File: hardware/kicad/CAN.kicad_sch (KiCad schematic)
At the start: 0 parts

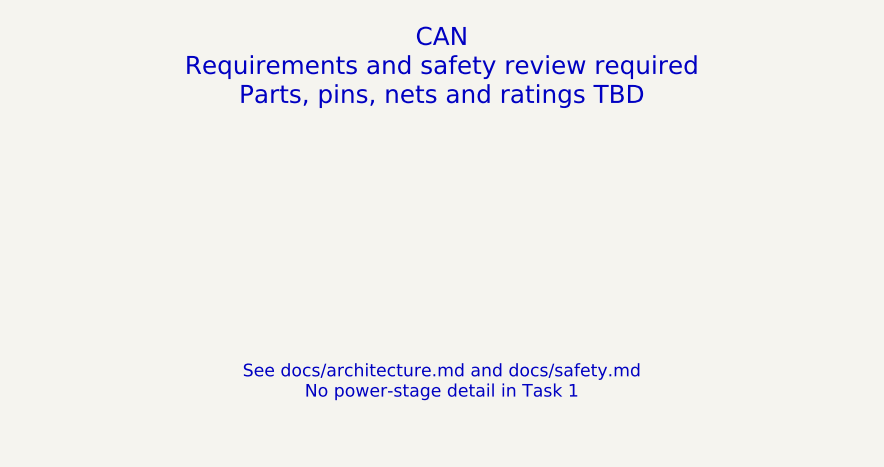
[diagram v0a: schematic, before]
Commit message: hardware: update existing KiCad architecture and add precharge sheet
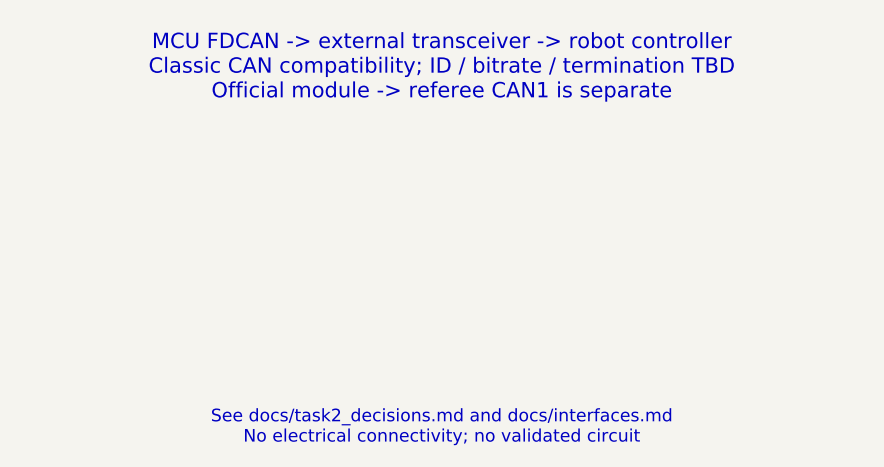
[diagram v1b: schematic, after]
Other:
- note added: "MCU FDCAN -> external transceiver -> robot controller Classic CAN compatibility; ID / bitrate / termination TBD Official module -> referee CAN1 is separate"
- note added: "See docs/task2_decisions.md and docs/interfaces.md No electrical connectivity; no validated circuit"
- note removed: "CAN Requirements and safety review required Parts, pins, nets and ratings TBD"
- note removed: "See docs/architecture.md and docs/safety.md No power-stage detail in Task 1"
- title: CAN - Placeholder -> CAN - Task 2 Proposal

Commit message: hardware: implement prototype Rev A electrical schematic
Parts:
- added C81: 100nF / 16V X7R, Capacitor_SMD:C_0805_2012Metric, symbol RevA:C
- added J19: robot telemetry CAN / official module CAN separate, symbol RevA:J3
- added J20: selectable termination shunt, fit only at bus end, Connector_PinHeader_2.54mm:PinHeader_1x02_P2.54mm_Vertical, symbol RevA:J2
- added R161, R162: 10k, Resistor_SMD:R_0805_2012Metric, symbol RevA:R
- added R163: 120R /1%, Resistor_SMD:R_0805_2012Metric, symbol RevA:R
- added U27: SN65HVD230DR, Package_SO:SOIC-8_3.9x4.9mm_P1.27mm, symbol RevA:SN65HVD230DR
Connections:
- new net CAN_H: J19.1 (P1), R163.1 (A), U27.7 (CANH)
- new net CAN_L: J19.2 (P2), J20.2 (P2), U27.6 (CANL)
- new net CAN_RX: U27.4 (R)
- new net CAN_STANDBY: R162.1 (A), U27.8 (RS)
- new net CAN_TERM: J20.1 (P1), R163.2 (B)
- new net CAN_TX: R161.1 (A), U27.1 (D)
- new net GND: C81.2 (B), J19.3 (P3), U27.2 (GND)
- new net V3V3: C81.1 (A), R161.2 (B), R162.2 (B), U27.3 (VCC)
- no-connect marks 0 -> 1
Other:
- note added: "CAN powered-off impedance/common-mode protection and external power through UART/SWD/taps require validation."
- note added: "Classic CAN initial protocol, bitrate/ID/timeouts TBD. CAN comm must not bypass official cutoff."
- note removed: "MCU FDCAN -> external transceiver -> robot controller Classic CAN compatibility; ID / bitrate / termination TBD Official module -> referee CAN1 is separate"
- note removed: "See docs/task2_decisions.md and docs/interfaces.md No electrical connectivity; no validated circuit"
- title: CAN - Task 2 Proposal -> CAN / Prototype Rev A draft

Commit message: hardware: refine Rev A protection and passive selections
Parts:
- removed C81: 100nF / 16V X7R, Capacitor_SMD:C_0805_2012Metric, symbol RevA:C
- removed J19: robot telemetry CAN / official module CAN separate, symbol RevA:J3
- removed J20: selectable termination shunt, fit only at bus end, Connector_PinHeader_2.54mm:PinHeader_1x02_P2.54mm_Vertical, symbol RevA:J2
- removed R161, R162: 10k, Resistor_SMD:R_0805_2012Metric, symbol RevA:R
- removed R163: 120R /1%, Resistor_SMD:R_0805_2012Metric, symbol RevA:R
- removed U27: SN65HVD230DR, Package_SO:SOIC-8_3.9x4.9mm_P1.27mm, symbol RevA:SN65HVD230DR
- added C99: 100nF / 16V X7R, Capacitor_SMD:C_0805_2012Metric, symbol RevA:C
- added J16: robot telemetry CAN / official module CAN separate, symbol RevA:J3
- added J17: selectable termination shunt, fit only at bus end, Connector_PinHeader_2.54mm:PinHeader_1x02_P2.54mm_Vertical, symbol RevA:J2
- added R167, R168: 10k, Resistor_SMD:R_0805_2012Metric, symbol RevA:R
- added R169: 120R /1%, Resistor_SMD:R_0805_2012Metric, symbol RevA:R
- added U33: SN65HVD230DR, Package_SO:SOIC-8_3.9x4.9mm_P1.27mm, symbol RevA:SN65HVD230DR
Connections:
- net CAN_H: now also J16.1 (P1), R169.1 (A), U33.7 (CANH)
- net CAN_L: now also J16.2 (P2), J17.2 (P2), U33.6 (CANL)
- net CAN_RX: now also U33.4 (R)
- net CAN_STANDBY: now also R168.1 (A), U33.8 (RS)
- net CAN_TERM: now also J17.1 (P1), R169.2 (B)
- net CAN_TX: now also R167.1 (A), U33.1 (D)
- net GND: now also C99.2 (B), J16.3 (P3), U33.2 (GND)
- net V3V3: now also C99.1 (A), R167.2 (B), R168.2 (B), U33.3 (VCC)
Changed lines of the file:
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@@
     (on_board yes)
     (dnp no)
-    (property "Reference" "U27" (at 88.9 102.95 0) (effects (font (size 1 1))))
+    (property "Reference" "U33" (at 88.9 102.95 0) (effects (font (size 1 1))))
     (property "Value" "SN65HVD230DR" (at 88.9 124.64999999999999 0) (effects (font (size 1 1))))
     (property "Footprint" "Package_SO:SOIC-8_3.9x4.9mm_P1.27mm" (at 88.9 114.3 0) (effects (font (size 1 1))) (hide yes))
     (property "Datasheet" "https://www.ti.com/lit/ds/symlink/sn65hvd230.pdf" (at 88.9 114.3 0) (effects (font (size 1 1))) (hide yes))
+    (property "MPN" "SN65HVD230DR" (at 88.9 114.3 0) (effects (font (size 1 1))) (hide yes))
     (pin "1")
     (pin "2")
@@
     (pin "7")
     (pin "8")
-    (instances (project "robomaster_supercap" (path "/fe0d835f-f536-483b-a54a-4b6f1f4699ec/f2d4b9a7-1a6d-5805-a86e-ee030607ac49" (reference "U27") (unit 1))))
+    (instances (project "robomaster_supercap" (path "/fe0d835f-f536-483b-a54a-4b6f1f4699ec/f2d4b9a7-1a6d-5805-a86e-ee030607ac49" (reference "U33") (unit 1))))
   )
   (wire (pts (xy 73.66 110.49) (xy 68.58 110.49)) (stroke (width 0) (type default)))
@@
     (on_board yes)
     (dnp no)
-    (property "Reference" "C81" (at 241.3 104.3 0) (effects (font (size 1 1))))
+    (property "Reference" "C99" (at 241.3 104.3 0) (effects (font (size 1 1))))
     (property "Value" "100nF / 16V X7R" (at 241.3 123.3 0) (effects (font (size 1 1))))
     (property "Footprint" "Capacitor_SMD:C_0805_2012Metric" (at 241.3 114.3 0) (effects (font (size 1 1))) (hide yes))
     (property "Datasheet" "" (at 241.3 114.3 0) (effects (font (size 1 1))) (hide yes))
+    (property "MPN" "C0805C104K5RACTU" (at 241.3 114.3 0) (effects (font (size 1 1))) (hide yes))
     (pin "1")
     (pin "2")
-    (instances (project "robomaster_supercap" (path "/fe0d835f-f536-483b-a54a-4b6f1f4699ec/f2d4b9a7-1a6d-5805-a86e-ee030607ac49" (reference "C81") (unit 1))))
+    (instances (project "robomaster_supercap" (path "/fe0d835f-f536-483b-a54a-4b6f1f4699ec/f2d4b9a7-1a6d-5805-a86e-ee030607ac49" (reference "C99") (unit 1))))
   )
   (wire (pts (xy 226.06 114.3) (xy 220.98 114.3)) (stroke (width 0) (type default)))
@@
     (on_board yes)
     (dnp no)
-    (property "Reference" "R161" (at 393.70000000000005 104.3 0) (effects (font (size 1 1))))
+    (property "Reference" "R167" (at 393.70000000000005 104.3 0) (effects (font (size 1 1))))
     (property "Value" "10k" (at 393.70000000000005 123.3 0) (effects (font (size 1 1))))
     (property "Footprint" "Resistor_SMD:R_0805_2012Metric" (at 393.70000000000005 114.3 0) (effects (font (size 1 1))) (hide yes))
     (property "Datasheet" "" (at 393.70000000000005 114.3 0) (effects (font (size 1 1))) (hide yes))
+    (property "MPN" "CRCW080510K0FKEA" (at 393.70000000000005 114.3 0) (effects (font (size 1 1))) (hide yes))
     (pin "1")
     (pin "2")
-    (instances (project "robomaster_supercap" (path "/fe0d835f-f536-483b-a54a-4b6f1f4699ec/f2d4b9a7-1a6d-5805-a86e-ee030607ac49" (reference "R161") (unit 1))))
+    (instances (project "robomaster_supercap" (path "/fe0d835f-f536-483b-a54a-4b6f1f4699ec/f2d4b9a7-1a6d-5805-a86e-ee030607ac49" (reference "R167") (unit 1))))
   )
   (wire (pts (xy 378.46 114.3) (xy 373.38 114.3)) (stroke (width 0) (type default)))
@@
     (on_board yes)
     (dnp no)
-    (property "Reference" "R162" (at 546.1 104.3 0) (effects (font (size 1 1))))
+    (property "Reference" "R168" (at 546.1 104.3 0) (effects (font (size 1 1))))
     (property "Value" "10k" (at 546.1 123.3 0) (effects (font (size 1 1))))
     (property "Footprint" "Resistor_SMD:R_0805_2012Metric" (at 546.1 114.3 0) (effects (font (size 1 1))) (hide yes))
     (property "Datasheet" "" (at 546.1 114.3 0) (effects (font (size 1 1))) (hide yes))
+    (property "MPN" "CRCW080510K0FKEA" (at 546.1 114.3 0) (effects (font (size 1 1))) (hide yes))
     (pin "1")
     (pin "2")
-    (instances (project "robomaster_supercap" (path "/fe0d835f-f536-483b-a54a-4b6f1f4699ec/f2d4b9a7-1a6d-5805-a86e-ee030607ac49" (reference "R162") (unit 1))))
+    (instances (project "robomaster_supercap" (path "/fe0d835f-f536-483b-a54a-4b6f1f4699ec/f2d4b9a7-1a6d-5805-a86e-ee030607ac49" (reference "R168") (unit 1))))
   )
   (wire (pts (xy 530.86 114.3) (xy 525.78 114.3)) (stroke (width 0) (type default)))
@@
     (on_board yes)
     (dnp no)
-    (property "Reference" "J19" (at 698.5 104.3 0) (effects (font (size 1 1))))
+    (property "Reference" "J16" (at 698.5 104.3 0) (effects (font (size 1 1))))
     (property "Value" "robot telemetry CAN / official module CAN separate" (at 698.5 123.3 0) (effects (font (size 1 1))))
     (property "Footprint" "" (at 698.5 114.3 0) (effects (font (size 1 1))) (hide yes))
     (property "Datasheet" "" (at 698.5 114.3 0) (effects (font (size 1 1))) (hide yes))
+    (property "MPN" "" (at 698.5 114.3 0) (effects (font (size 1 1))) (hide yes))
     (pin "1")
     (pin "2")
     (pin "3")
-    (instances (project "robomaster_supercap" (path "/fe0d835f-f536-483b-a54a-4b6f1f4699ec/f2d4b9a7-1a6d-5805-a86e-ee030607ac49" (reference "J19") (unit 1))))
+    (instances (project "robomaster_supercap" (path "/fe0d835f-f536-483b-a54a-4b6f1f4699ec/f2d4b9a7-1a6d-5805-a86e-ee030607ac49" (reference "J16") (unit 1))))
   )
   (wire (pts (xy 683.26 113.03) (xy 678.18 113.03)) (stroke (width 0) (type default)))
@@
     (on_board yes)
     (dnp no)
-    (property "Reference" "R163" (at 850.9 104.3 0) (effects (font (size 1 1))))
+    (property "Reference" "R169" (at 850.9 104.3 0) (effects (font (size 1 1))))
     (property "Value" "120R /1%" (at 850.9 123.3 0) (effects (font (size 1 1))))
     (property "Footprint" "Resistor_SMD:R_0805_2012Metric" (at 850.9 114.3 0) (effects (font (size 1 1))) (hide yes))
     (property "Datasheet" "" (at 850.9 114.3 0) (effects (font (size 1 1))) (hide yes))
+    (property "MPN" "CRCW0805120RFKEA" (at 850.9 114.3 0) (effects (font (size 1 1))) (hide yes))
     (pin "1")
     (pin "2")
-    (instances (project "robomaster_supercap" (path "/fe0d835f-f536-483b-a54a-4b6f1f4699ec/f2d4b9a7-1a6d-5805-a86e-ee030607ac49" (reference "R163") (unit 1))))
+    (instances (project "robomaster_supercap" (path "/fe0d835f-f536-483b-a54a-4b6f1f4699ec/f2d4b9a7-1a6d-5805-a86e-ee030607ac49" (reference "R169") (unit 1))))
   )
   (wire (pts (xy 835.66 114.3) (xy 830.58 114.3)) (stroke (width 0) (type default)))
@@
     (on_board yes)
     (dnp no)
-    (property "Reference" "J20" (at 1003.3000000000001 104.3 0) (effects (font (size 1 1))))
+    (property "Reference" "J17" (at 1003.3000000000001 104.3 0) (effects (font (size 1 1))))
     (property "Value" "selectable termination shunt, fit only at bus end" (at 1003.3000000000001 123.3 0) (effects (font (size 1 1))))
     (property "Footprint" "Connector_PinHeader_2.54mm:PinHeader_1x02_P2.54mm_Vertical" (at 1003.3000000000001 114.3 0) (effects (font (size 1 1))) (hide yes))
     (property "Datasheet" "" (at 1003.3000000000001 114.3 0) (effects (font (size 1 1))) (hide yes))
+    (property "MPN" "" (at 1003.3000000000001 114.3 0) (effects (font (size 1 1))) (hide yes))
     (pin "1")
     (pin "2")
-    (instances (project "robomaster_supercap" (path "/fe0d835f-f536-483b-a54a-4b6f1f4699ec/f2d4b9a7-1a6d-5805-a86e-ee030607ac49" (reference "J20") (unit 1))))
+    (instances (project "robomaster_supercap" (path "/fe0d835f-f536-483b-a54a-4b6f1f4699ec/f2d4b9a7-1a6d-5805-a86e-ee030607ac49" (reference "J17") (unit 1))))
   )
   (wire (pts (xy 988.06 114.3) (xy 982.98 114.3)) (stroke (width 0) (type default)))
